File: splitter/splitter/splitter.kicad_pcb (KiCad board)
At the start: 2 copper layers, 60 x 63 mm, 25 parts, among them J1 JACKIN, J2 JACKSEND, J3 JACKRCV, J4 JACKOUT, J5 Jack-DC, SW1 SW_HIGHLOW, SW2 SW_POWER, U1 TL074, U2 TLE2426xLP

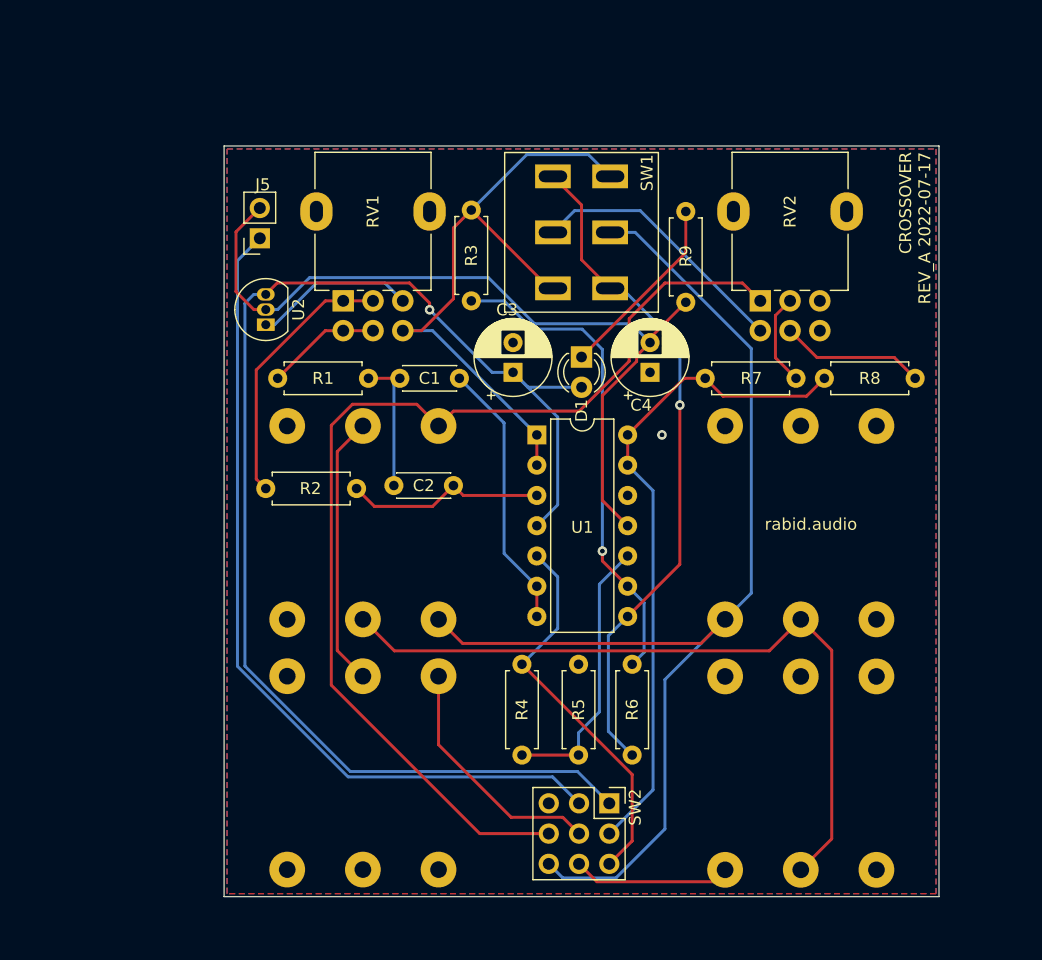
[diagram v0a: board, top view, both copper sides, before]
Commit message: rework switches to allow low/high/all send and bypass
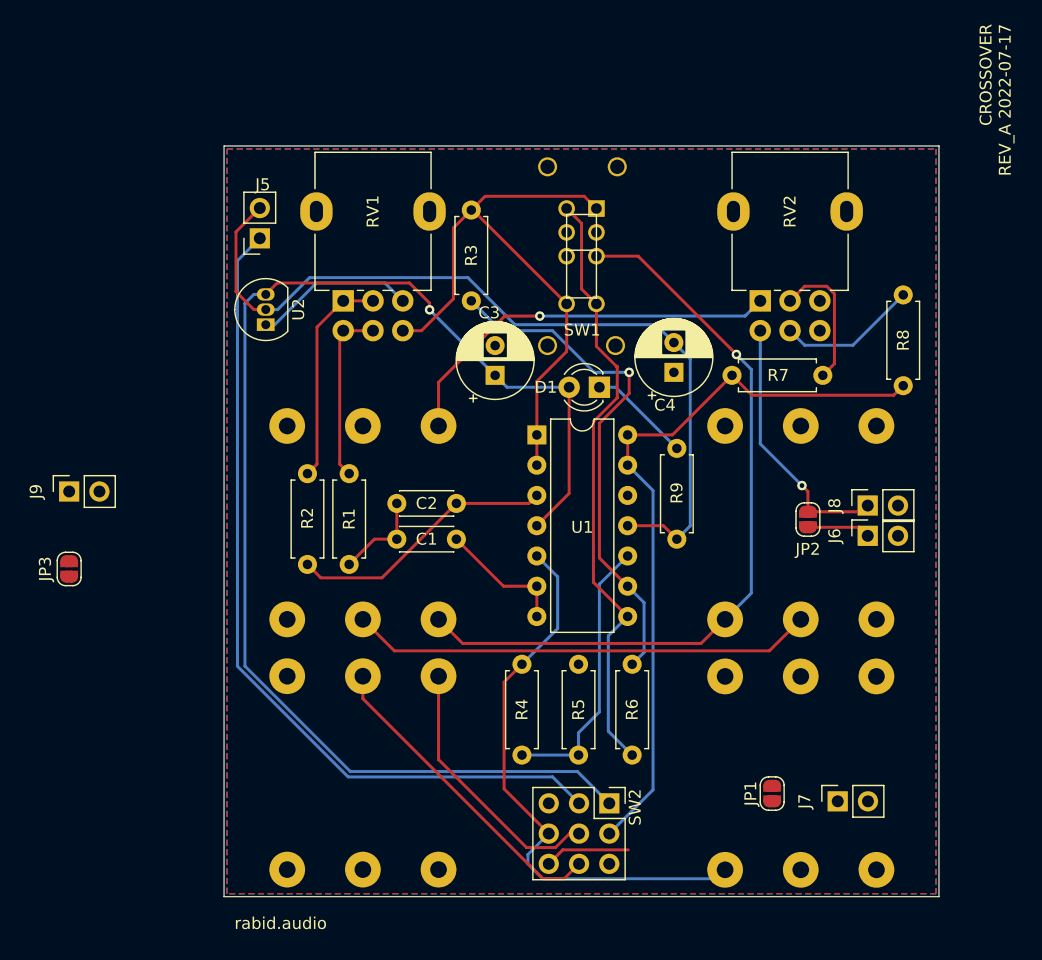
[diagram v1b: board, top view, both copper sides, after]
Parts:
- added J6: SEND_DRY, Connector_PinSocket_2.54mm:PinSocket_1x02_P2.54mm_Vertical, F.Cu at (54.0, 41.2)
- added J7: RING_SEND, Connector_PinSocket_2.54mm:PinSocket_1x02_P2.54mm_Vertical, F.Cu at (51.5, 63.5)
- added J8: RECV_DRY, Connector_PinSocket_2.54mm:PinSocket_1x02_P2.54mm_Vertical, F.Cu at (54.0, 38.7)
- added J9: RING_RECV, Connector_PinSocket_2.54mm:PinSocket_1x02_P2.54mm_Vertical, F.Cu at (-13.0, 37.5)
- added JP1: JMP_RING_SEND, Jumper:SolderJumper-2_P1.3mm_Open_RoundedPad1.0x1.5mm, F.Cu at (46.0, 62.9)
- added JP2: JMP_DRY, Jumper:SolderJumper-2_P1.3mm_Open_RoundedPad1.0x1.5mm, F.Cu at (49.0, 39.9)
- added JP3: JMP_RING_RECV, Jumper:SolderJumper-2_P1.3mm_Open_RoundedPad1.0x1.5mm, F.Cu at (-13.0, 44.0)
- J3: value JACKRCV -> JACKRECV
- SW1: value SW_HIGHLOW -> SW_MODE; footprint Button_Switch_THT:MTS-200_DPDT_6T -> Button_Switch_THT:SW_EG2301_DP3T
- SW2: value SW_POWER -> SW_BYPASS
- moved R9 19.9 mm to (38.0, 33.9)
- moved C1 13.5 mm to (14.5, 41.5)
- moved R1 10.0 mm to (10.5, 36.0), turned to 270 degrees
- moved R8 7.07 mm to (57.0, 21.0), turned to 270 degrees
- moved R2 3.72 mm to (7.00, 36.0), turned to 270 degrees
- moved D1 2.95 mm to (31.5, 28.8), turned to 180 degrees
- moved SW1 2.93 mm to (31.2, 13.8)
- moved R7 2.26 mm to (50.2, 27.8)
- moved C4 2.00 mm to (37.8, 27.5)
- moved C2 1.52 mm to (19.5, 38.5)
- moved C3 1.52 mm to (22.8, 27.8)
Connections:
- J1 pad R: /SEND_R -> Net-(J1-PadR)
- J1 pad T: Net-(J1-PadT) -> /IN
- J2 pad R: /SEND_R -> Net-(J2-PadR)
- J2 pad T: /SEND_T -> /SEND_WET
- J3 pad R: /RECV_R -> Net-(J3-PadR)
- J3 pad RN: /SEND_R -> Net-(J2-PadR)
- J3 pad T: /RECV_T -> /RECV_WET
- J3 pad TN: /SEND_T -> /SEND_WET
- J4 pad R: /RECV_R -> Net-(J4-PadR)
- RV2 pad 1: /RECV_T -> /RECV_WET
- RV2 pad 4: /DRY_SIG -> /RECV_DRY
- SW1 pad 2: /SEND_T -> /IN
- SW1 pad 3: /LOW -> /SEND_WET
- SW1 pad 5: /DRY_SIG -> /LOW
- SW1 pad 6: /HIGH -> GND
- SW2 pad 6: /RECV_T -> /IN
- SW2 pad 7: /IN -> Net-(JP3-Pad2)
- SW2 pad 8: Net-(J1-PadT) -> Net-(J4-PadR)
- SW2 pad 9: /SEND_T -> Net-(J1-PadR)
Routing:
- net /SEND_T: track 96.9 -> 0.00 mm
- net /RECV_T: track 90.4 -> 0.00 mm
- net /SEND_WET: track 0.00 -> 64.5 mm, vias 0 -> 1
- net /SEND_R: track 62.1 -> 0.00 mm
- net Net-(J2-PadR): track 0.00 -> 38.9 mm
- net /RECV_WET: track 0.00 -> 33.5 mm, vias 0 -> 1
- net Net-(J4-PadR): track 0.00 -> 26.8 mm
- net /RECV_R: track 22.8 -> 0.00 mm
- net /DRY_SIG: track 22.3 -> 0.00 mm
- net /RECV_DRY: track 0.00 -> 22.1 mm, vias 0 -> 1
- net /IN: track 32.4 -> 49.5 mm
- net Net-(J1-PadT): track 13.3 -> 0.00 mm
- net Net-(C1-Pad2): track 22.7 -> 10.9 mm
- net Net-(D1-Pad1): track 15.8 -> 8.62 mm
- net Net-(J1-PadR): track 0.00 -> 7.16 mm
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
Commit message: fix some bugs
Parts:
- added R10: 1M, Resistor_THT:R_Axial_DIN0207_L6.3mm_D2.5mm_P7.62mm_Horizontal, F.Cu at (48.0, 35.5)
- C1, C2: value 220n -> 22n
- J1: value JACKIN -> IN
- J2: value JACKSEND -> SEND
- J3: value JACKRECV -> RECV
- J4: value JACKOUT -> OUT
- J6: value SEND_DRY -> CONN_SEND_DRY
- J8: value RECV_DRY -> CONN_RECV_DRY
- RV2: value A1M_DUAL_MIX -> MIX
- moved JP3 34.0 mm to (14.0, 64.7), turned to 90 degrees
- moved J9 33.8 mm to (8.00, 64.0), turned to 270 degrees
- moved J6 31.6 mm to (36.1, 15.2), turned to 180 degrees
- moved J8 28.1 mm to (38.6, 15.2), turned to 180 degrees
- moved R6 25.7 mm to (43.0, 35.5), turned to 270 degrees
- moved JP2 23.4 mm to (37.4, 19.5), turned to 0 degrees
- moved R5 7.83 mm to (32.0, 59.5), turned to 90 degrees
- moved R4 2.50 mm to (27.5, 59.5)
- moved J7 1.80 mm to (50.0, 62.5)
- moved R9 1.62 mm to (38.0, 35.5)
- moved C3 0.25 mm to (22.5, 27.8)
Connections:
- R7 pad 2: /OUT -> Net-(R10-Pad1)
- R8 pad 2: /OUT -> Net-(R10-Pad1)
- RV2 pad 1: /RECV_WET -> GND
- RV2 pad 2: Net-(R7-Pad1) -> Net-(R8-Pad1)
- RV2 pad 3: GND -> /RECV_DRY
- RV2 pad 4: /RECV_DRY -> /RECV_WET
- RV2 pad 5: Net-(R8-Pad1) -> Net-(R7-Pad1)
- U1 pad 10: Net-(R4-Pad1) -> GND
- U1 pad 12: GND -> Net-(R4-Pad1)
- U1 pad 13: /OUT -> Net-(R3-Pad1)
- U1 pad 14: /OUT -> /LOW
- U1 pad 8: /LOW -> /OUT
- U1 pad 9: Net-(R3-Pad1) -> Net-(R10-Pad1)
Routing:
- net Net-(R10-Pad1): track 0.00 -> 43.5 mm
- net Net-(J3-PadR): track 0.00 -> 40.1 mm
- net /IN: track 49.5 -> 76.7 mm
- net /OUT: track 62.1 -> 36.8 mm
- net Net-(JP3-Pad2): track 0.00 -> 21.7 mm
- net Net-(J1-PadR): track 7.16 -> 27.7 mm
- net Net-(J2-PadR): track 38.9 -> 57.5 mm
- net /LOW: track 51.2 -> 33.2 mm
- net /SEND_DRY: track 5.32 -> 19.2 mm
- net GND: track 14.2 -> 0.86 mm, vias 0 -> 2
- net Net-(R3-Pad1): track 43.4 -> 35.3 mm
- net Net-(R7-Pad1): track 11.7 -> 4.89 mm
- net GNDD: track 70.7 -> 75.9 mm
- net /RECV_DRY: track 22.1 -> 17.3 mm, vias 1 -> 0
- net /SEND_WET: track 64.5 -> 60.8 mm, vias 1 -> 0
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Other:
- board text added: "REV.A CROSSOVER 2022-07-17"
- board text removed: "CROSSOVER REV_A 2022-07-17"

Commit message: bug fixes
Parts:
- J1: value IN -> JACKIN
- J2: value SEND -> JACKSEND
- J3: value RECV -> JACKRECV
- J4: value OUT -> JACKOUT
- R7, R8: value 1M -> 470K
- RV2: footprint Potentiometer_THT:Potentiometer_Alpha_RD902F-40-00D_Dual_Vertical -> Potentiometer_THT:Potentiometer_Alpha_RD901F-40-00D_Single_Vertical
- moved R8 7.02 mm to (56.5, 28.0), turned to 90 degrees
- moved R7 6.27 mm to (44.0, 28.2), turned to 0 degrees
- moved U2 4.50 mm to (3.50, 28.0)
- moved RV1 3.75 mm to (10.0, 25.2)
- moved RV2 3.75 mm to (45.0, 25.2)
- moved J5 1.78 mm to (3.50, 18.0), turned to 0 degrees
- renumbered R9 to R10, R10 to R9
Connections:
- R7 pad 1: Net-(R7-Pad1) -> /RECV_WET
- R7 pad 2: Net-(R10-Pad1) -> Net-(R7-Pad2)
- R8 pad 2: Net-(R10-Pad1) -> /RECV_DRY
- R9 pad 1: Net-(R10-Pad1) -> Net-(R9-Pad1)
- RV1 pad 2: Net-(R2-Pad1) -> GND
- RV1 pad 5: Net-(R1-Pad1) -> /HIGH
- RV2 pad 1: GND -> Net-(R8-Pad1)
- RV2 pad 2: Net-(R8-Pad1) -> Net-(R9-Pad1)
- RV2 pad 3: /RECV_DRY -> Net-(R7-Pad2)
- U1 pad 9: Net-(R10-Pad1) -> Net-(R9-Pad1)
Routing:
- net Net-(R10-Pad1): track 43.5 -> 0.00 mm
- net Net-(R9-Pad1): track 0.00 -> 33.1 mm
- net +9V: track 112.9 -> 106.0 mm, vias 1 -> 0
- net Net-(R2-Pad1): track 18.2 -> 12.0 mm
- net Net-(R1-Pad1): track 15.0 -> 8.71 mm
- net /RECV_DRY: track 17.3 -> 23.4 mm
- net Net-(R7-Pad1): track 4.89 -> 0.00 mm
- net /HIGH: track 52.6 -> 57.3 mm
- net GNDD: track 75.9 -> 71.6 mm
- net Net-(R7-Pad2): track 0.00 -> 3.67 mm
- net Net-(R8-Pad1): track 10.4 -> 13.7 mm
- net Net-(J5-Pad1): track 70.1 -> 68.6 mm
- net /RECV_WET: track 36.3 -> 37.1 mm

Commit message: cleanup
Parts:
- C3, C4: value 10u -> .1u
- RV2: value MIX -> B1M_MIX
- moved C4 0.25 mm to (37.5, 27.5)
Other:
- board text added: "9V+"

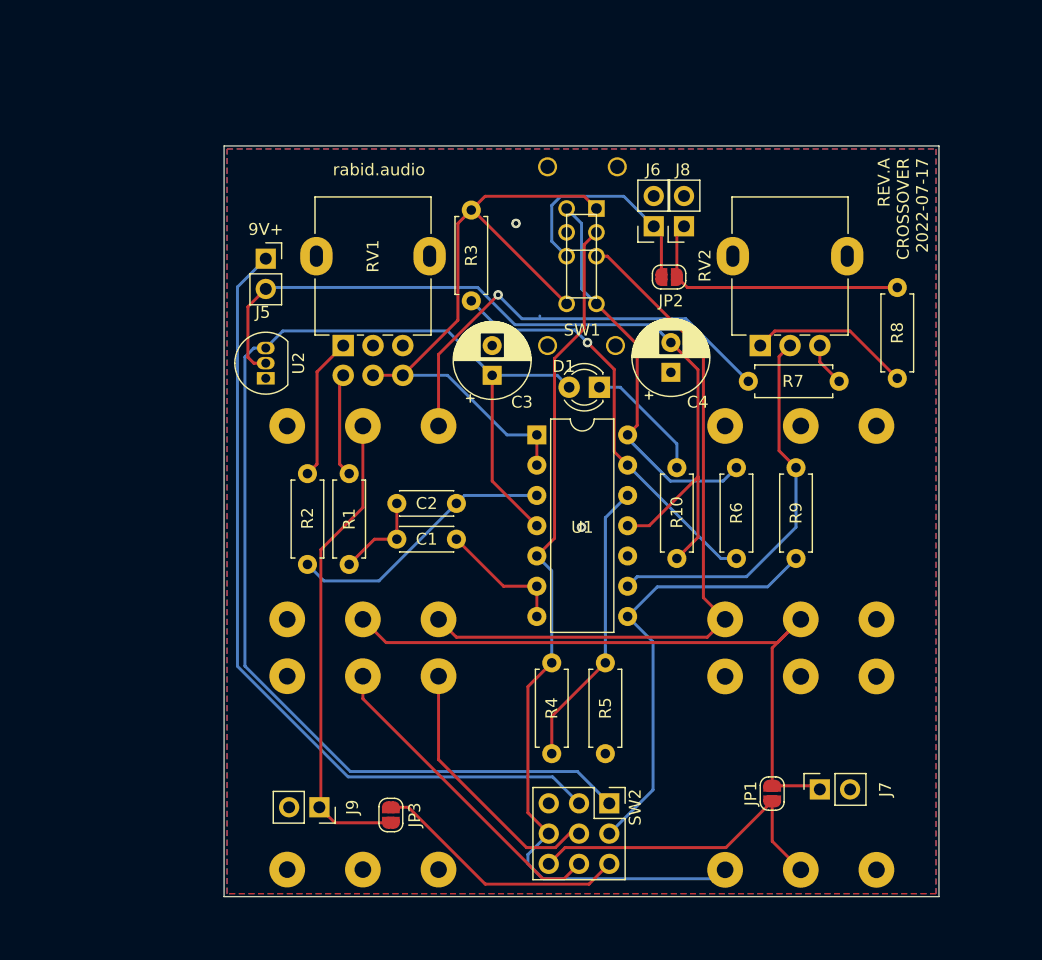
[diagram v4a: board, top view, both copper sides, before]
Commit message: rev b based on learnings from assembly
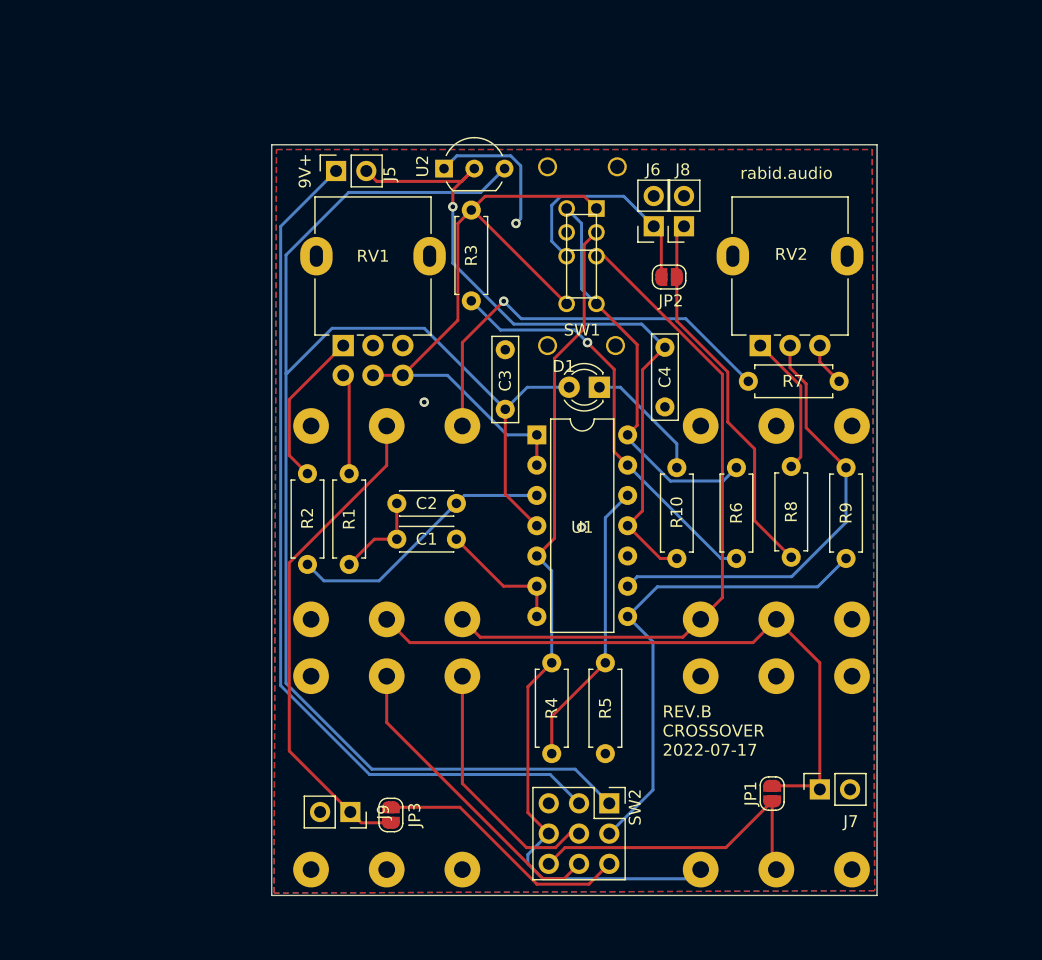
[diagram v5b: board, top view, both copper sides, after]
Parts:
- C3, C4: footprint Capacitor_THT:CP_Radial_D6.3mm_P2.50mm -> Capacitor_THT:C_Rect_L7.0mm_W2.0mm_P5.00mm
- U2: footprint Package_TO_SOT_THT:TO-92_Inline -> Package_TO_SOT_THT:TO-92_Inline_Wide
- moved U2 23.1 mm to (18.5, 10.4), turned to 0 degrees
- moved R8 11.6 mm to (47.6, 35.4), turned to 270 degrees
- moved J5 9.43 mm to (9.40, 10.6), turned to 90 degrees
- moved R9 4.20 mm to (52.2, 35.5)
- moved C3 3.05 mm to (23.6, 30.6)
- moved C4 2.94 mm to (37.0, 30.4)
- moved J9 2.63 mm to (10.6, 64.4)
- moved J1 2.05 mm to (40.0, 69.2)
- moved J2 2.05 mm to (40.0, 48.2)
- moved J3 2.00 mm to (20.0, 32.0)
- moved J4 2.00 mm to (20.0, 53.0)
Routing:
- net +9V: track 106.0 -> 128.6 mm
- net GND: track 0.86 -> 12.6 mm, vias 2 -> 3
- net GNDD: track 71.6 -> 60.8 mm, vias 0 -> 1
- net /RECV_DRY: track 23.4 -> 32.0 mm
- net Net-(J5-Pad1): track 68.6 -> 74.2 mm
- net Net-(R9-Pad1): track 33.1 -> 37.5 mm
- net /OUT: track 36.8 -> 41.0 mm
- net /SEND_WET: track 60.9 -> 57.2 mm
- net /IN: track 76.7 -> 73.2 mm
- net Net-(J2-PadR): track 57.5 -> 54.2 mm
- net /RECV_WET: track 37.1 -> 35.2 mm
- net Net-(R8-Pad1): track 13.7 -> 11.9 mm
- net Net-(J3-PadR): track 40.1 -> 41.7 mm
- net Net-(R2-Pad1): track 12.0 -> 13.3 mm
- net Net-(J1-PadR): track 27.7 -> 26.8 mm
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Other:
- board size 60 x 63 mm -> 50.8 x 63 mm
- board text added: "REV.B CROSSOVER 2022-07-17"
- board text removed: "REV.A CROSSOVER 2022-07-17"

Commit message: rev B
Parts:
- R10: value 220 -> 1k
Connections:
- J4 pad RN: GND -> Net-(J4-PadRN)
- J4 pad TN: GND -> Net-(J4-PadTN)
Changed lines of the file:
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@@
     (zones 0)
     (modules 33)
-    (nets 33)
+    (nets 35)
   )
   (page A4)
@@
   (net 31 "Net-(R7-Pad2)")
   (net 32 "Net-(R9-Pad1)")
+  (net 33 "Net-(J4-PadTN)")
+  (net 34 "Net-(J4-PadRN)")
   (net_class Default "This is the default net class."
     (clearance 0.2)
@@
     (add_net "Net-(J3-PadR)")
     (add_net "Net-(J4-PadR)")
+    (add_net "Net-(J4-PadRN)")
     (add_net "Net-(J4-PadT)")
+    (add_net "Net-(J4-PadTN)")
     (add_net "Net-(J5-Pad1)")
     (add_net "Net-(JP3-Pad2)")
@@
       (effects (font (size 1 1) (thickness 0.15)))
     )
+    (fp_line (start 0.74 1.85) (end 4.34 1.85) (layer F.SilkS) (width 0.12))
+    (fp_line (start 0.8 1.75) (end 4.3 1.75) (layer F.Fab) (width 0.1))
+    (fp_line (start -1.01 -2.73) (end 6.09 -2.73) (layer F.CrtYd) (width 0.05))
+    (fp_line (start -1.01 -2.73) (end -1.01 2.01) (layer F.CrtYd) (width 0.05))
+    (fp_line (start 6.09 2.01) (end 6.09 -2.73) (layer F.CrtYd) (width 0.05))
+    (fp_line (start 6.09 2.01) (end -1.01 2.01) (layer F.CrtYd) (width 0.05))
     (fp_arc (start 2.54 0) (end 4.34 1.85) (angle -20) (layer F.SilkS) (width 0.12))
     (fp_arc (start 2.54 0) (end 2.54 -2.48) (angle -135) (layer F.Fab) (width 0.1))
@@
       (effects (font (size 1 1) (thickness 0.15)))
     )
-    (fp_line (start 0.74 1.85) (end 4.34 1.85) (layer F.SilkS) (width 0.12))
-    (fp_line (start 0.8 1.75) (end 4.3 1.75) (layer F.Fab) (width 0.1))
-    (fp_line (start -1.01 -2.73) (end 6.09 -2.73) (layer F.CrtYd) (width 0.05))
-    (fp_line (start -1.01 -2.73) (end -1.01 2.01) (layer F.CrtYd) (width 0.05))
-    (fp_line (start 6.09 2.01) (end 6.09 -2.73) (layer F.CrtYd) (width 0.05))
-    (fp_line (start 6.09 2.01) (end -1.01 2.01) (layer F.CrtYd) (width 0.05))
     (pad 1 thru_hole rect (at 0 0 90) (size 1.5 1.5) (drill 0.8) (layers *.Cu *.Mask)
       (net 4 GND))
@@
       (effects (font (size 1 1) (thickness 0.15)))
     )
-    (fp_text value 220 (at 6 0 180) (layer F.Fab)
+    (fp_text value 1k (at 6 0 180) (layer F.Fab)
       (effects (font (size 1 1) (thickness 0.15)))
     )
@@
     )
     (pad TN thru_hole circle (at 0 -16.23 180) (size 3 3) (drill 1.4) (layers *.Cu *.Mask)
-      (net 4 GND))
+      (net 33 "Net-(J4-PadTN)"))
     (pad SN thru_hole circle (at 12.7 -16.23 180) (size 3 3) (drill 1.4) (layers *.Cu *.Mask)
       (net 4 GND))
     (pad RN thru_hole circle (at 6.35 -16.23 180) (size 3 3) (drill 1.4) (layers *.Cu *.Mask)
-      (net 4 GND))
+      (net 34 "Net-(J4-PadRN)"))
     (pad T thru_hole circle (at 0 0 180) (size 3 3) (drill 1.4) (layers *.Cu *.Mask)
       (net 10 "Net-(J4-PadT)"))
@@
   (segment (start 19.535001 9.324999) (end 24.056001 9.324999) (width 0.25) (layer B.Cu) (net 4))
   (segment (start 18.46 10.4) (end 19.535001 9.324999) (width 0.25) (layer B.Cu) (net 4) (status 10))
+  (segment (start 8 64) (end 8.125001 63.874999) (width 0.25) (layer F.Cu) (net 4) (status 30))
   (segment (start 32.33 63.67) (end 32.134998 63.67) (width 0.25) (layer B.Cu) (net 5) (status 30))
   (segment (start 25.45 28.75) (end 23.6 30.6) (width 0.25) (layer B.Cu) (net 5) (status 20))
@@
   (segment (start 38.75 23) (end 44 28.25) (width 0.25) (layer B.Cu) (net 25) (status 20))
   (segment (start 24.940308 23) (end 38.75 23) (width 0.25) (layer B.Cu) (net 25))
-  (segment (start 8 64) (end 8.125001 63.874999) (width 0.25) (layer F.Cu) (net 4) (status 30))
   (segment (start 13.65 35.304998) (end 5.474999 43.479999) (width 0.25) (layer F.Cu) (net 26))
   (segment (start 13.65 32) (end 13.65 35.304998) (width 0.25) (layer F.Cu) (net 26) (status 10))

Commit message: cleanup
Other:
- board text added: "21mm between jacks 61.5mm internal width, 2mm walls"
- board text removed: "21mm between jacks 61.5mm internal width, 2mm walls, 60mm board width jack sleve 4mm. thus needs 2-(1.5/2) = 1.25mm inset"
